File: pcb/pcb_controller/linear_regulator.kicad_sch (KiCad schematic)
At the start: 24 parts, among them IC301 OPA277, IC302 OPA277, Q304 BC557

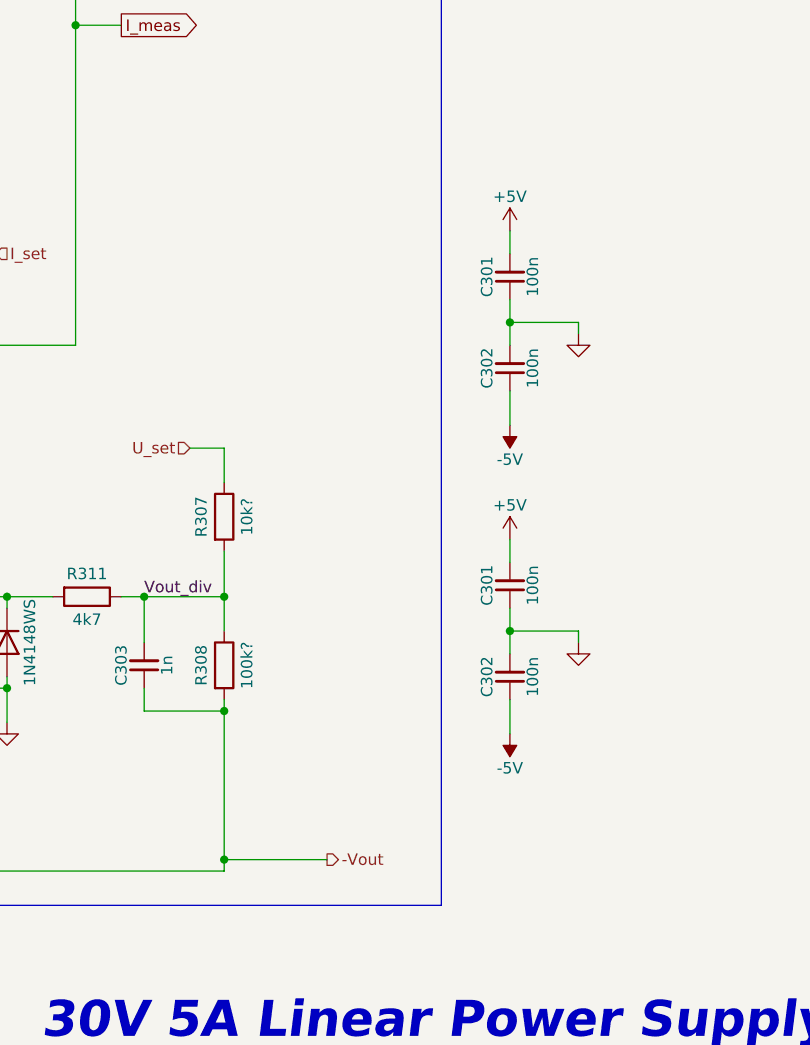
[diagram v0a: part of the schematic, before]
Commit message: kicad 8.0
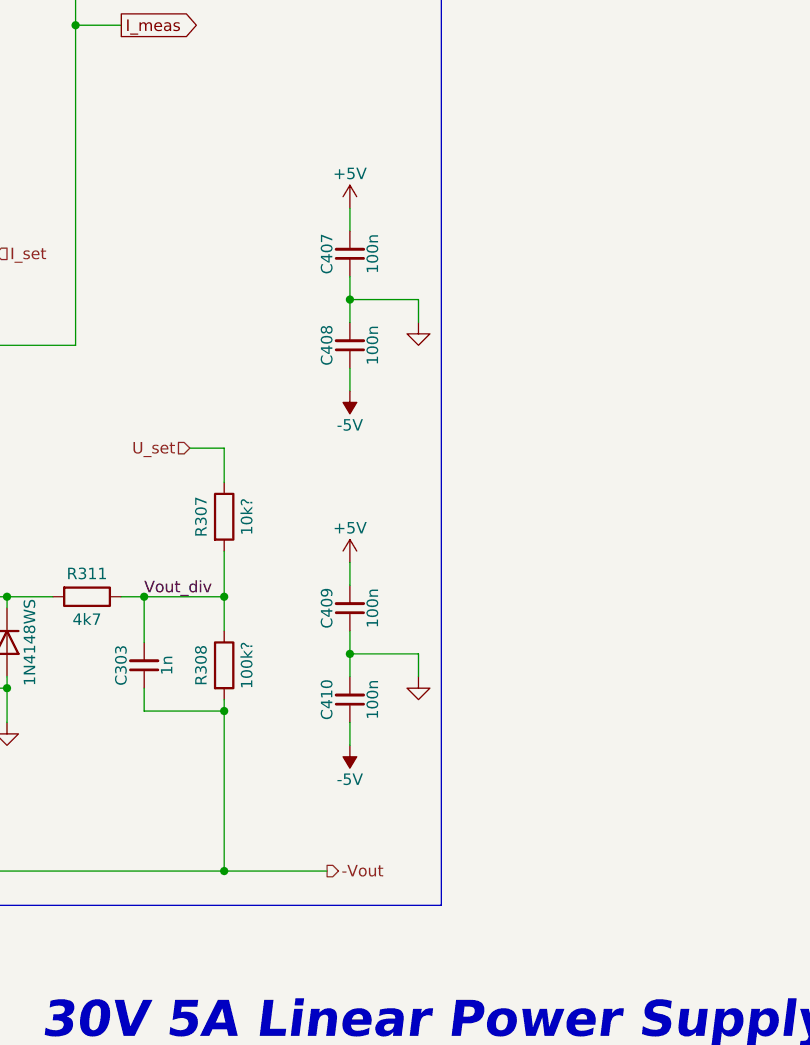
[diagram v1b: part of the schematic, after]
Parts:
- renumbered C301 to C407, C302 to C408, C301 to C409, C302 to C410
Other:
- moved on the sheet: C407, C408, C409, C410

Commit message: most analog layout
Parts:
- added C604: 10u, Capacitor_THT:CP_Radial_D5.0mm_P2.00mm, symbol Device:C_Polarized_Small
- Q304: value BC557 -> S9015
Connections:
- net +5V: now also C409.1; no longer C409.2
- net -5V: now also C408.2, C410.2; no longer C408.1, C410.1
- net -Vin: now also C604.2
- net GND: now also C408.1, C409.2, C410.1, C604.1; no longer C408.2, C409.1, C410.2
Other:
- moved on the sheet: C301, C302, C303, C304, C407, C408, C409, C410, D301, D302, D303, D304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

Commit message: minor changes
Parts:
- added D300: RED, LED_THT:LED_D5.0mm, symbol Device:LED
- added Q306: S9015, Package_TO_SOT_SMD:SOT-23, symbol Transistor_BJT:BC557
- added R324: 4k7, Resistor_SMD:R_0603_1608Metric, symbol Device:R
- added R325: 220R, Resistor_SMD:R_0603_1608Metric, symbol Device:R
- added U305: LM393, symbol Comparator:LM393
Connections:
- net +5V: now also Q306.3 (E)
- net GND: now also D300.1 (K)
- net out_CC_amp: now also R324.1
- new net: D300.2 (A), R325.1
- new net: Q306.1 (C), R325.2
- new net: Q306.2 (B), R324.2
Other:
- company: (none) -> Dominik Workshop
- title: (none) -> Main linear regulator
